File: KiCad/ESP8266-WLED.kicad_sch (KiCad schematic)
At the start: 6 parts, among them J1 USB_C_Receptacle_USB2.0_14P, U1 ESP-12F

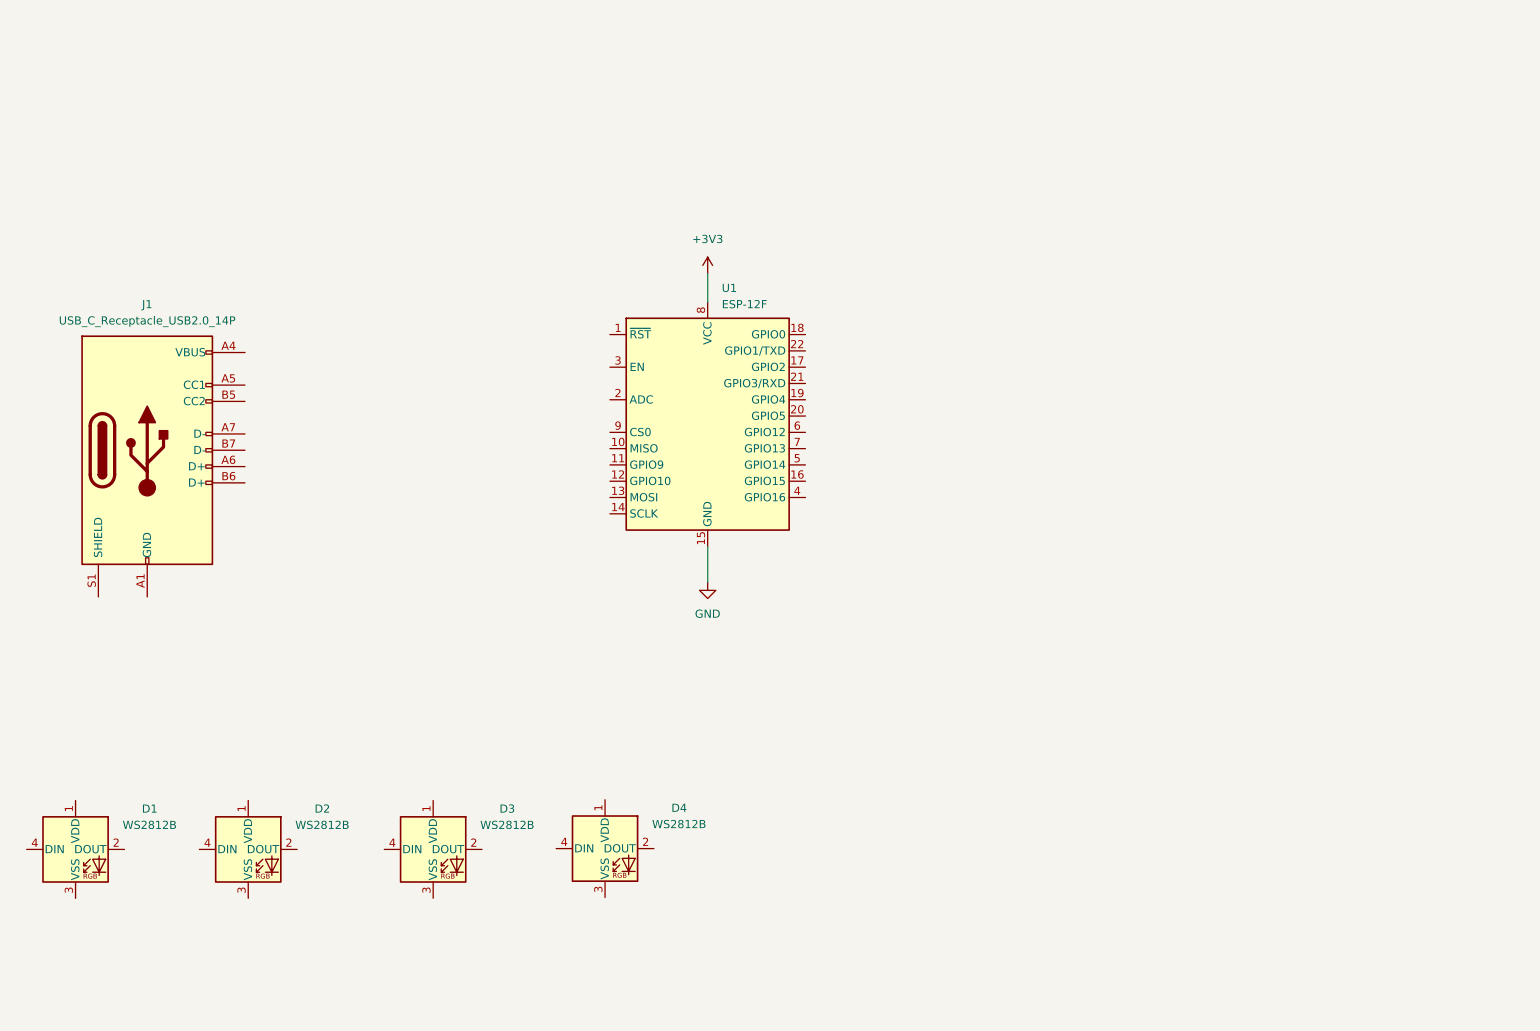
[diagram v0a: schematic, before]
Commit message: adding power supply, etc.
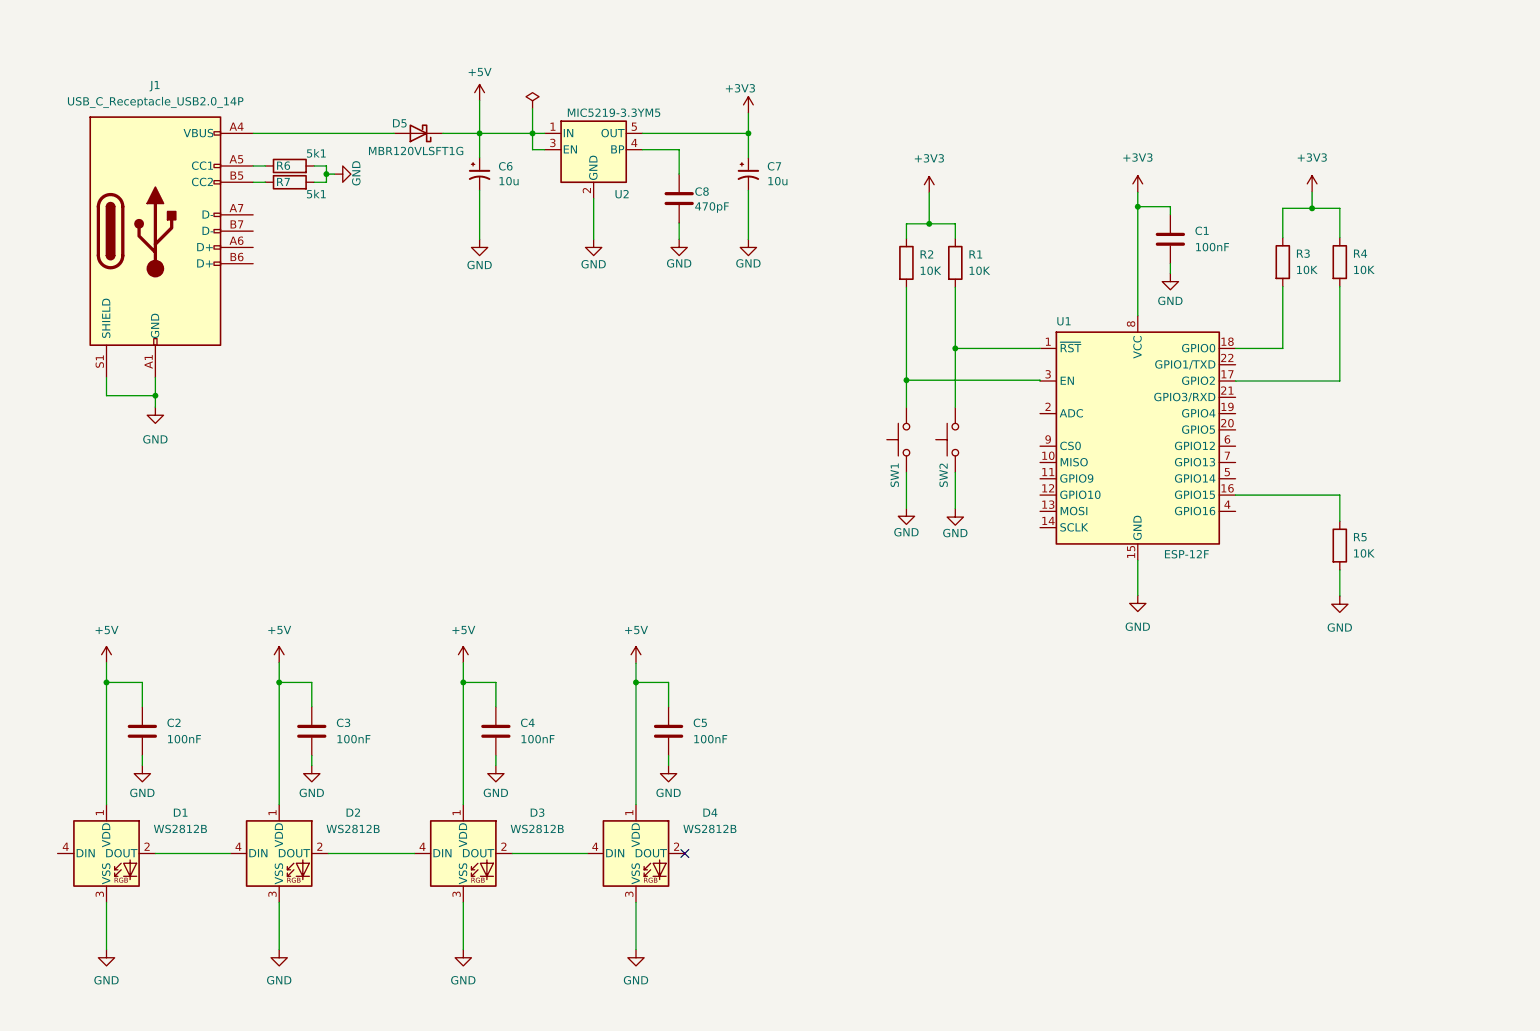
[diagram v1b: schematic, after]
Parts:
- added C1, C2, C3, C4, C5: 100nF, Capacitor_SMD:C_0603_1608Metric, symbol Device:C
- added C6, C7: 10u, Capacitor_SMD:C_1206_3216Metric, symbol Device:C_Polarized_Small_US
- added C8: 470pF, Capacitor_SMD:C_0603_1608Metric, symbol Device:C
- added D5: MBR120VLSFT1G, Diode_SMD:D_SOD-123F, symbol Device:D_Schottky
- added R1, R2, R3, R4, R5: 10K, Resistor_SMD:R_0603_1608Metric, symbol Device:R
- added R6, R7: 5k1, Resistor_SMD:R_0603_1608Metric, symbol Device:R
- added SW1, SW2: SW_Push, Button_Switch_SMD:SW_SPST_B3U-1000P, symbol Switch:SW_Push
- added U2: MIC5219-3.3YM5, Package_TO_SOT_SMD:SOT-23-5, symbol Regulator_Linear:MIC5219-3.3YM5
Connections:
- net +3V3: now also C1.1, C7.1, R1.1, R2.1, R3.1, R4.1, U2.5 (OUT)
- net GND: now also D1.3 (VSS), D2.3 (VSS), D3.3 (VSS), D4.3 (VSS), J1.A1 (GND), J1.A12 (GND), J1.B1 (GND), J1.B12 (GND), J1.S1 (SHIELD), C1.2, C2.2, C3.2, C4.2, C5.2, C6.2, C7.2, C8.2, R5.2, R6.2, R7.2, SW1.1, SW2.1, U2.2 (GND)
- net +5V: now reaches D4.1 (VDD)
- net +5V: now also D1.1 (VDD), D2.1 (VDD), D3.1 (VDD), C2.1, C3.1, C4.1, C5.1, C6.1, D5.1 (K), U2.1 (IN), U2.3 (EN)
- net at D4.4 (DIN): now also D3.2 (DOUT)
- net at D2.2 (DOUT): now also D3.4 (DIN)
- net at D2.4 (DIN): now also D1.2 (DOUT)
- net at U1.1 (~{RST}): now also R1.2, SW2.2
- net at U1.16 (GPIO15): now also R5.1
- net at U1.17 (GPIO2): now also R4.2
- net at U1.18 (GPIO0): now also R3.2
- net at U1.3 (EN): now also R2.2, SW1.2
- net at J1.A4 (VBUS), J1.A9 (VBUS), J1.B4 (VBUS)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: now also D5.2 (A)
- net at J1.A5 (CC1): now also R6.1
- net at J1.B5 (CC2): now also R7.1
- new net: C8.1, U2.4 (BP)
- no-connect marks 0 -> 1
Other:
- moved on the sheet: D1, D2, D3, D4, J1, U1

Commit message: adding serial interface
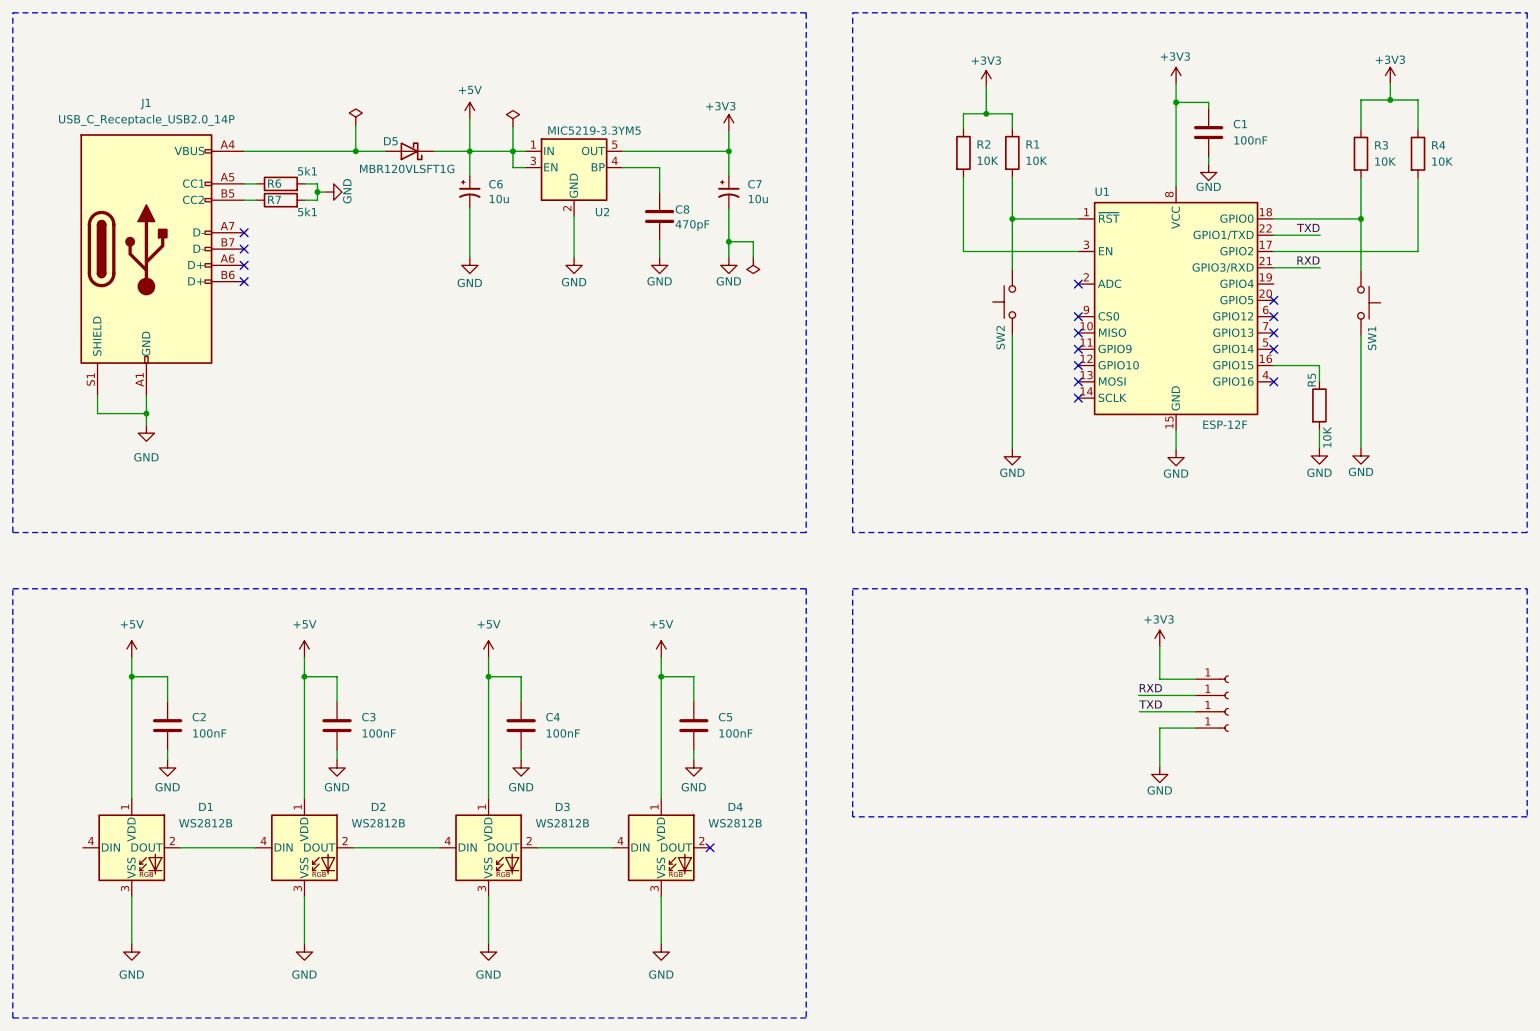
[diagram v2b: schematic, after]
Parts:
- added J2, J3, J4, J5: Conn_01x01_Socket, TestPoint:TestPoint_Pad_D1.5mm, symbol Connector:Conn_01x01_Socket
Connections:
- net +3V3: now also J2.1 (Pin_1)
- net GND: now also J5.1 (Pin_1)
- net at R2.2, U1.3 (EN): no longer SW1.2
- net at R3.2, U1.18 (GPIO0): now also SW1.2
- net RXD: now reaches U1.21 (GPIO3/RXD)
- net RXD: now also J3.1 (Pin_1)
- net TXD: now reaches U1.22 (GPIO1/TXD)
- net TXD: now also J4.1 (Pin_1)
- no-connect marks 1 -> 17
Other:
- moved on the sheet: C1, C2, C3, C4, C5, C6, C7, C8, D1, D2, D3, D4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

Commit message: First time finalizing the schematic and fixing all errors
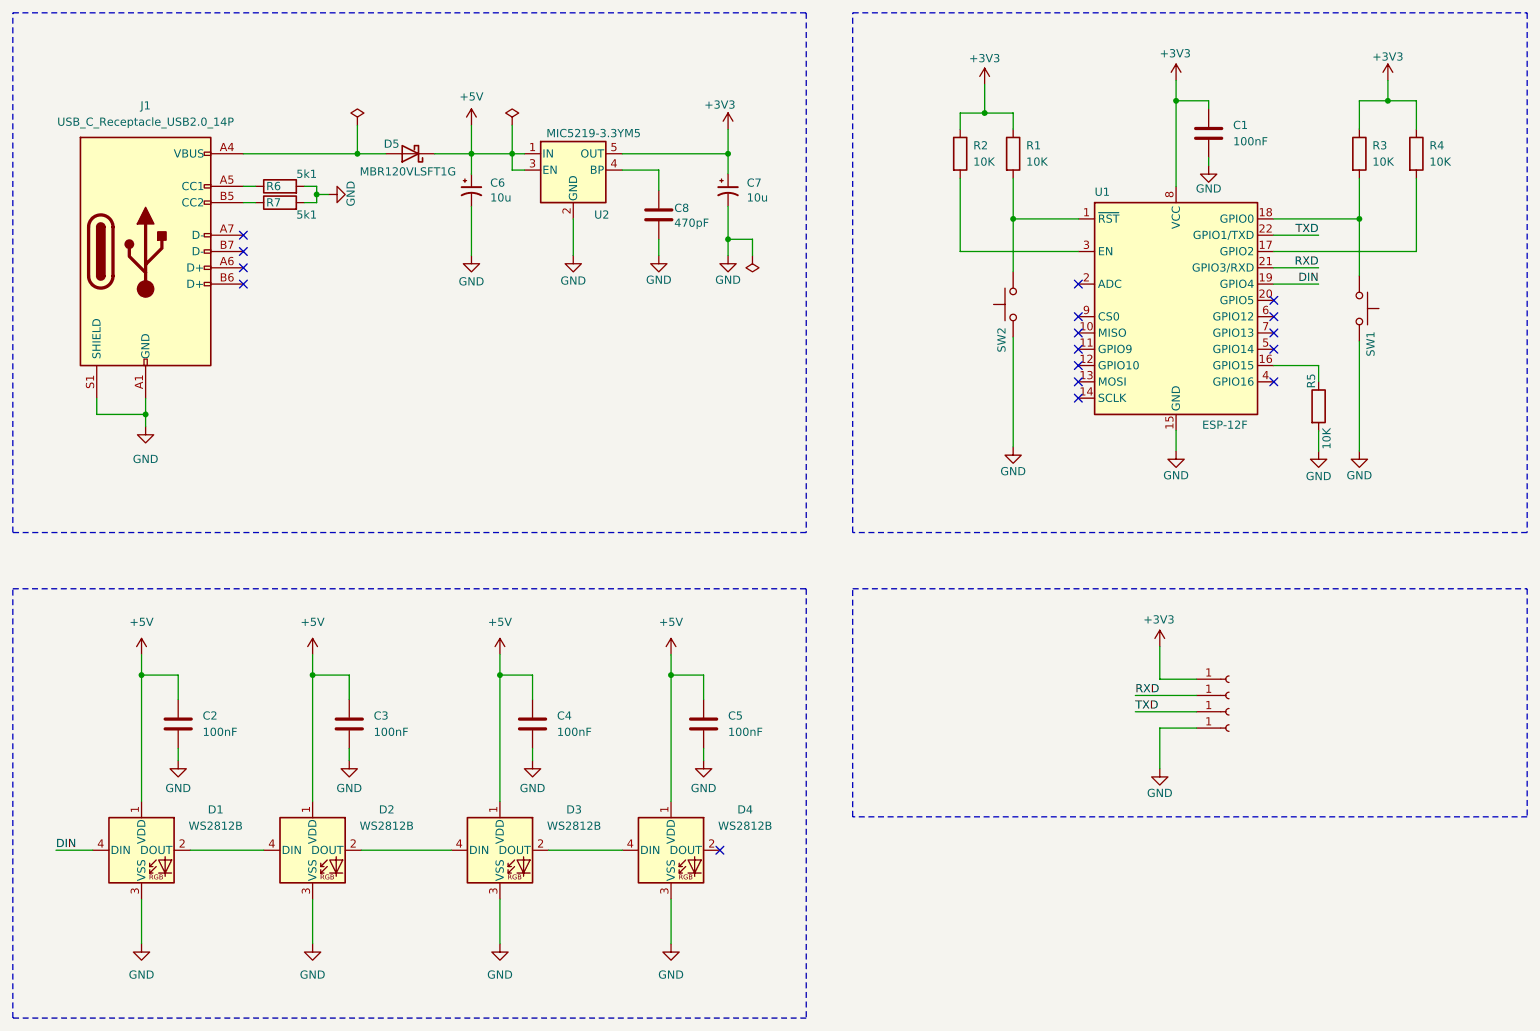
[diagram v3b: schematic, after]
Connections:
- net DIN: now reaches U1.19 (GPIO4)
- net DIN: now also D1.4 (DIN)
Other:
- moved on the sheet: C2, C3, C4, C5, D1, D2, D3, D4, R2, SW1

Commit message: first time everything routed
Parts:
- removed D5: MBR120VLSFT1G, Diode_SMD:D_SOD-123F, symbol Device:D_Schottky
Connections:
- net +5V: now also J1.A4 (VBUS), J1.A9 (VBUS), J1.B4 (VBUS), J1.B9 (VBUS)
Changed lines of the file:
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@@
 	)
 	(junction
-		(at 85.09 51.435)
-		(diameter 0)
-		(color 0 0 0 0)
-	)
-	(junction
 		(at 182.88 45.085)
 		(diameter 0)
@@
 	(wire
 		(pts
-			(xy 85.09 51.435) (xy 89.535 51.435)
+			(xy 67.31 51.435) (xy 102.87 51.435)
 		)
 		(stroke
@@
 	(wire
 		(pts
-			(xy 85.09 46.99) (xy 85.09 51.435)
-		)
-		(stroke
-			(width 0)
-			(type default)
-		)
-	)
-	(wire
-		(pts
 			(xy 206.375 135.89) (xy 215.9 135.89)
 		)
@@
 	(wire
 		(pts
-			(xy 67.31 51.435) (xy 85.09 51.435)
-		)
-		(stroke
-			(width 0)
-			(type default)
-		)
-	)
-	(wire
-		(pts
 			(xy 51.435 129.54) (xy 51.435 132.715)
 		)
@@
 		)
 	)
-	(wire
-		(pts
-			(xy 97.155 51.435) (xy 102.87 51.435)
-		)
-		(stroke
-			(width 0)
-			(type default)
-		)
-	)
 	(rectangle
 		(start 162.306 29.464)
@@
 	)
 	(symbol
-		(lib_id "Device:D_Schottky")
-		(at 93.345 51.435 180)
-		(unit 1)
-		(exclude_from_sim no)
-		(in_bom yes)
-		(on_board yes)
-		(dnp no)
-		(property "Reference" "D5"
-			(at 90.424 49.911 0)
-			(effects
-				(font
-					(size 1.27 1.27)
-				)
-			)
-		)
-		(property "Value" "MBR120VLSFT1G"
-			(at 92.964 54.229 0)
-			(effects
-				(font
-					(size 1.27 1.27)
-				)
-			)
-		)
-		(property "Footprint" "Diode_SMD:D_SOD-123F"
-			(at 93.345 51.435 0)
-			(effects
-				(font
-					(size 1.27 1.27)
-				)
-				(hide yes)
-			)
-		)
-		(property "Datasheet" "~"
-			(at 93.345 51.435 0)
-			(effects
-				(font
-					(size 1.27 1.27)
-				)
-				(hide yes)
-			)
-		)
-		(property "Description" ""
-			(at 93.345 51.435 0)
-			(effects
-				(font
-					(size 1.27 1.27)
-				)
-				(hide yes)
-			)
-		)
-		(property "LCSC" "C235756"
-			(at 90.424 49.911 0)
-			(effects
-				(font
-					(size 1.27 1.27)
-				)
-				(hide yes)
-			)
-		)
-		(pin "2"
-		)
-		(pin "1"
-		)
-		(instances
-			(project "ESP8266-WLED"
-				(path "/a2ef812b-ccda-4368-828d-0f9caf70d413"
-					(reference "D5")
-					(unit 1)
-				)
-			)
-		)
-	)
-	(symbol
 		(lib_id "power:+3V3")
 		(at 212.725 40.005 0)
@@
 					(unit 1)
 				)
-			)
-		)
-	)
-	(symbol
-		(lib_id "power:PWR_FLAG")
-		(at 85.09 46.99 0)
-		(unit 1)
-		(exclude_from_sim no)
-		(in_bom yes)
-		(on_board yes)
-		(dnp no)
-		(fields_autoplaced yes)
-		(property "Reference" "#FLG02"
-			(at 85.09 45.085 0)
-			(effects
-				(font
-					(size 1.27 1.27)
-				)
-				(hide yes)
-			)
-		)
-		(property "Value" "PWR_FLAG"
-			(at 85.09 42.545 0)
-			(effects
-				(font
-					(size 1.27 1.27)
-				)
-				(hide yes)
-			)
-		)
-		(property "Footprint" ""
-			(at 85.09 46.99 0)
-			(effects
-				(font
-					(size 1.27 1.27)
-				)
-				(hide yes)
-			)
-		)
-		(property "Datasheet" "~"
-			(at 85.09 46.99 0)
-			(effects
-				(font
-					(size 1.27 1.27)
-				)
-				(hide yes)
-			)
-		)
-		(property "Description" "Special symbol for telling ERC where power comes from"
-			(at 85.09 46.99 0)
-			(effects
-				(font
-					(size 1.27 1.27)
-				)
-				(hide yes)
-			)
-		)
-		(pin "1"
-		)
-		(instances
-			(project "ESP8266-WLED"
-				(path "/a2ef812b-ccda-4368-828d-0f9caf70d413"
-					(reference "#FLG02")
-					(unit 1)
-				)
